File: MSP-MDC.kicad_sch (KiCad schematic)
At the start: 4 parts, among them J1 Conn_01x24_Pin, J2 Conn_01x12_Pin, J3 Conn_01x24_Pin

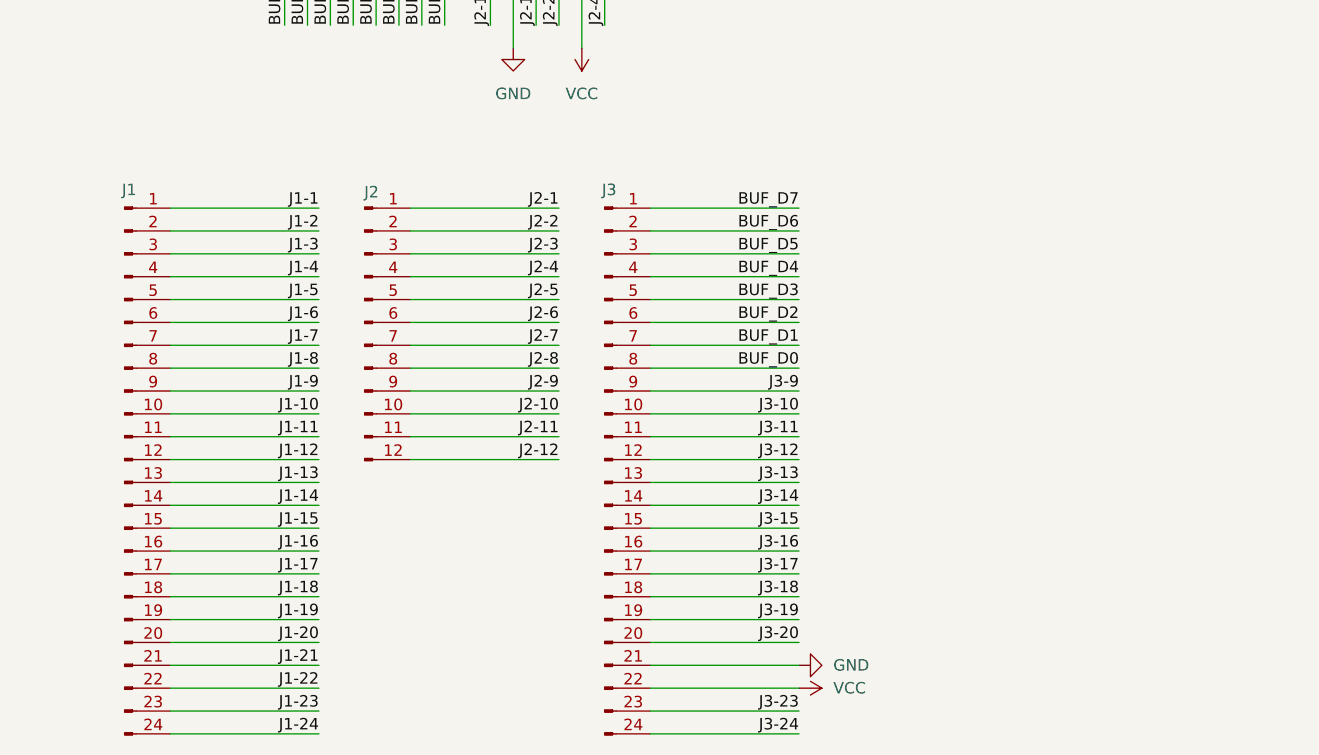
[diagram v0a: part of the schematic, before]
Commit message: Added some basic traces for power
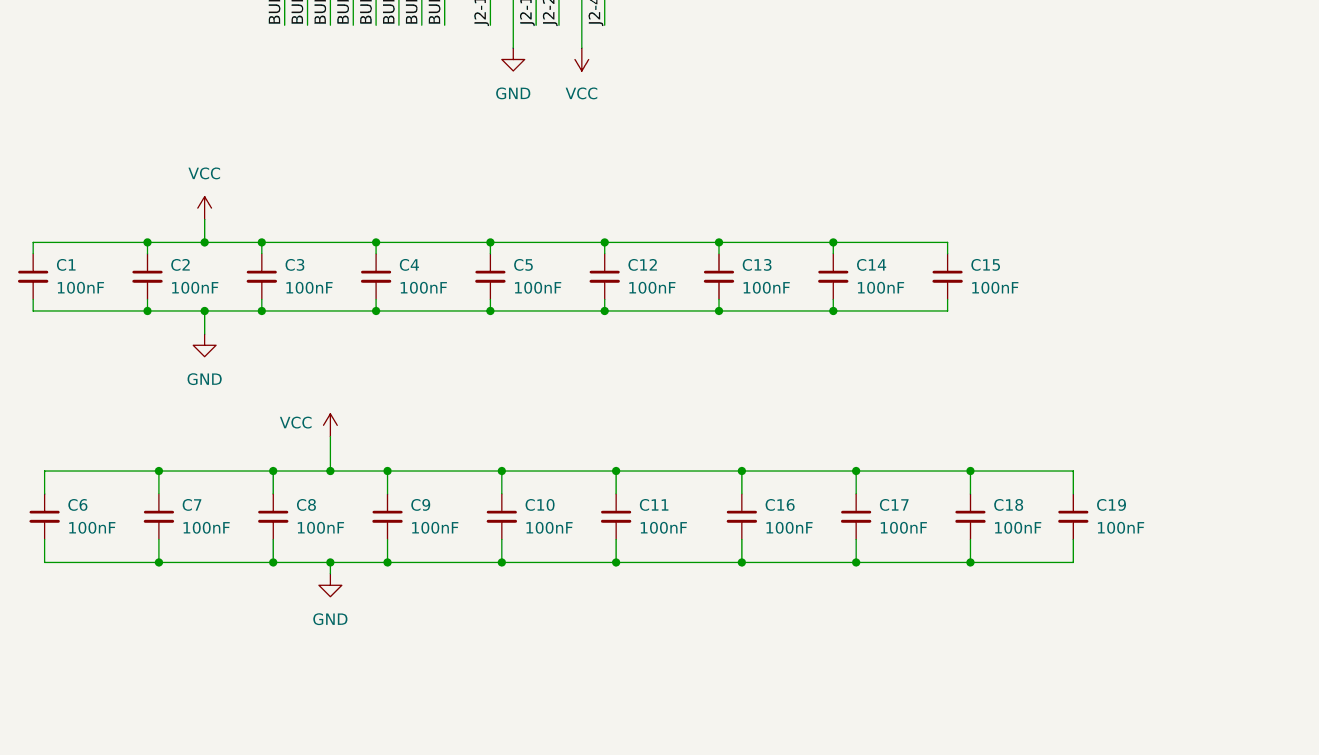
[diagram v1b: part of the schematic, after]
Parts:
- removed J1, J3: Conn_01x24_Pin, symbol Connector:Conn_01x24_Pin
- removed J2: Conn_01x12_Pin, symbol Connector:Conn_01x12_Pin
- added C1, C10, C11, C12, C13, C14, C15, C16, C17, C18, C19, C2, C3, C4, C5, C6, C7, C8, C9: 100nF, Capacitor_SMD:C_1206_3216Metric_Pad1.33x1.80mm_HandSolder, symbol Device:C_Small
- U1: footprint (none) -> Wink:MSP-MDC
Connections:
- net GND: now also C1.2, C10.2, C11.2, C12.2, C13.2, C14.2, C15.2, C16.2, C17.2, C18.2, C19.2, C2.2, C3.2, C4.2, C5.2, C6.2, C7.2, C8.2, C9.2
- net VCC: now also C1.1, C10.1, C11.1, C12.1, C13.1, C14.1, C15.1, C16.1, C17.1, C18.1, C19.1, C2.1, C3.1, C4.1, C5.1, C6.1, C7.1, C8.1, C9.1

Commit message: Update board fixing adder issues
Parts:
- added RN1: 10K, Resistor_THT:R_Array_SIP9, symbol Device:R_Network08
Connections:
- net BUF_D0: now also RN1.2 (R1)
- net BUF_D1: now also RN1.3 (R2)
- net BUF_D2: now also RN1.4 (R3)
- net BUF_D3: now also RN1.5 (R4)
- net BUF_D4: now also RN1.6 (R5)
- net BUF_D5: now also RN1.7 (R6)
- net BUF_D6: now also RN1.8 (R7)
- net BUF_D7: now also RN1.9 (R8)
- net GND: now also RN1.1 (common)
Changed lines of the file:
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@@
 	(wire
 		(pts
+			(xy 66.04 107.95) (xy 66.04 110.49)
+		)
+		(stroke
+			(width 0)
+			(type default)
+		)
+	)
+	(wire
+		(pts
 			(xy 124.46 147.32) (xy 124.46 149.86)
 		)
@@
 	)
 	(symbol
+		(lib_id "Device:R_Network08")
+		(at 55.88 102.87 180)
+		(unit 1)
+		(exclude_from_sim no)
+		(in_bom yes)
+		(on_board yes)
+		(dnp no)
+		(property "Reference" "RN1"
+			(at 42.164 103.886 0)
+			(effects
+				(font
+					(size 1.27 1.27)
+				)
+				(justify right)
+			)
+		)
+		(property "Value" "10K"
+			(at 42.164 101.346 0)
+			(effects
+				(font
+					(size 1.27 1.27)
+				)
+				(justify right)
+			)
+		)
+		(property "Footprint" "Resistor_THT:R_Array_SIP9"
+			(at 43.815 102.87 90)
+			(effects
+				(font
+					(size 1.27 1.27)
+				)
+				(hide yes)
+			)
+		)
+		(property "Datasheet" "http://www.vishay.com/docs/31509/csc.pdf"
+			(at 55.88 102.87 0)
+			(effects
+				(font
+					(size 1.27 1.27)
+				)
+				(hide yes)
+			)
+		)
+		(property "Description" "8 resistor network, star topology, bussed resistors, small symbol"
+			(at 55.88 102.87 0)
+			(effects
+				(font
+					(size 1.27 1.27)
+				)
+				(hide yes)
+			)
+		)
+		(pin "3"
+		)
+		(pin "7"
+		)
+		(pin "2"
+		)
+		(pin "1"
+		)
+		(pin "6"
+		)
+		(pin "8"
+		)
+		(pin "5"
+		)
+		(pin "4"
+		)
+		(pin "9"
+		)
+		(instances
+			(project ""
+				(path "/6f5335a8-66b5-468f-92d4-becfba378f22"
+					(reference "RN1")
+					(unit 1)
+				)
+			)
+		)
+	)
+	(symbol
 		(lib_id "Device:C_Small")
 		(at 20.32 125.73 0)
@@
 					(unit 1)
 				)
+			)
+		)
+	)
+	(symbol
+		(lib_id "power:GND")
+		(at 66.04 110.49 0)
+		(unit 1)
+		(exclude_from_sim no)
+		(in_bom yes)
+		(on_board yes)
+		(dnp no)
+		(fields_autoplaced yes)
+		(property "Reference" "#PWR050"
+			(at 66.04 116.84 0)
+			(effects
+				(font
+					(size 1.27 1.27)
+				)
+				(hide yes)
+			)
+		)
+		(property "Value" "GND"
+			(at 66.04 115.57 0)
+			(effects
+				(font
+					(size 1.27 1.27)
+				)
+			)
+		)
+		(property "Footprint" ""
+			(at 66.04 110.49 0)
+			(effects
+				(font
+					(size 1.27 1.27)
+				)
+				(hide yes)
+			)
+		)
+		(property "Datasheet" ""
+			(at 66.04 110.49 0)
+			(effects
+				(font
+					(size 1.27 1.27)
+				)
+				(hide yes)
+			)
+		)
+		(property "Description" "Power symbol creates a global label with name \"GND\" , ground"
+			(at 66.04 110.49 0)
+			(effects
+				(font
+					(size 1.27 1.27)
+				)
+				(hide yes)
+			)
+		)
+		(pin "1"
+		)
+		(instances
+			(project "MSP-MDC"
+				(path "/6f5335a8-66b5-468f-92d4-becfba378f22"
+					(reference "#PWR050")
+					(unit 1)
+				)
